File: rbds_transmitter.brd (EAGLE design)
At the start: 160 x 100 mm, 136 parts, among them J2 AVRISP-6, Q1 P-CH, Q2 P-Ch, Q3 P-Ch, T1 ATB3225-75032CT, T2 ATB3225-75032CT, U1 MAX2606, U2 TS974, U3 TS974, U4 MAX1551, U5 ATMEGA328, U6 TPS61030, U7 MCP4812, X1 16Mhz

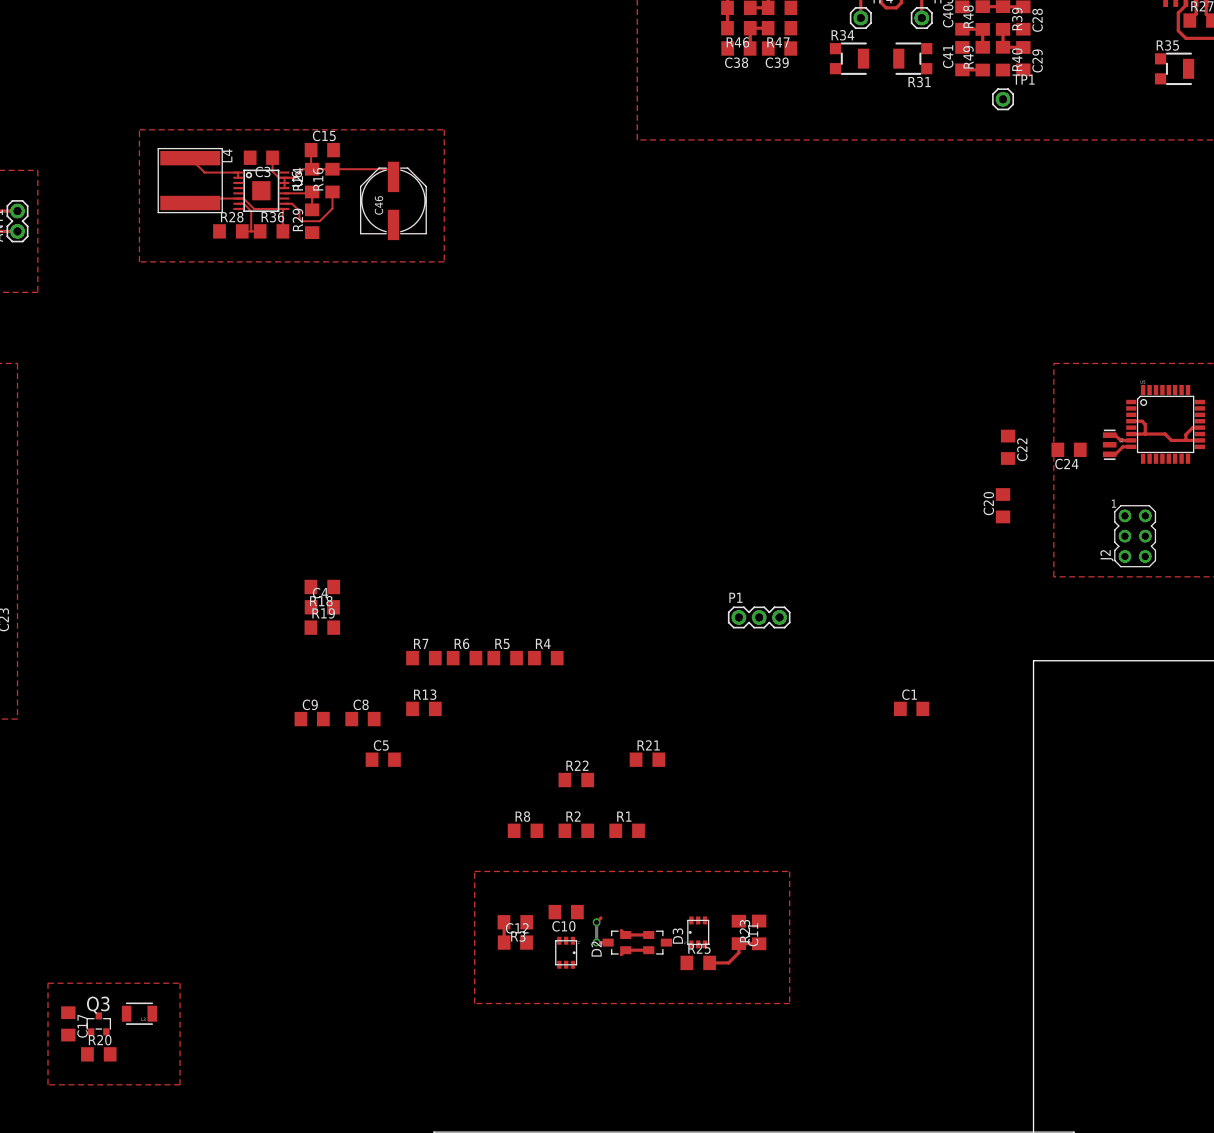
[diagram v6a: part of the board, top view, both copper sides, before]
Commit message: layed out some more traces
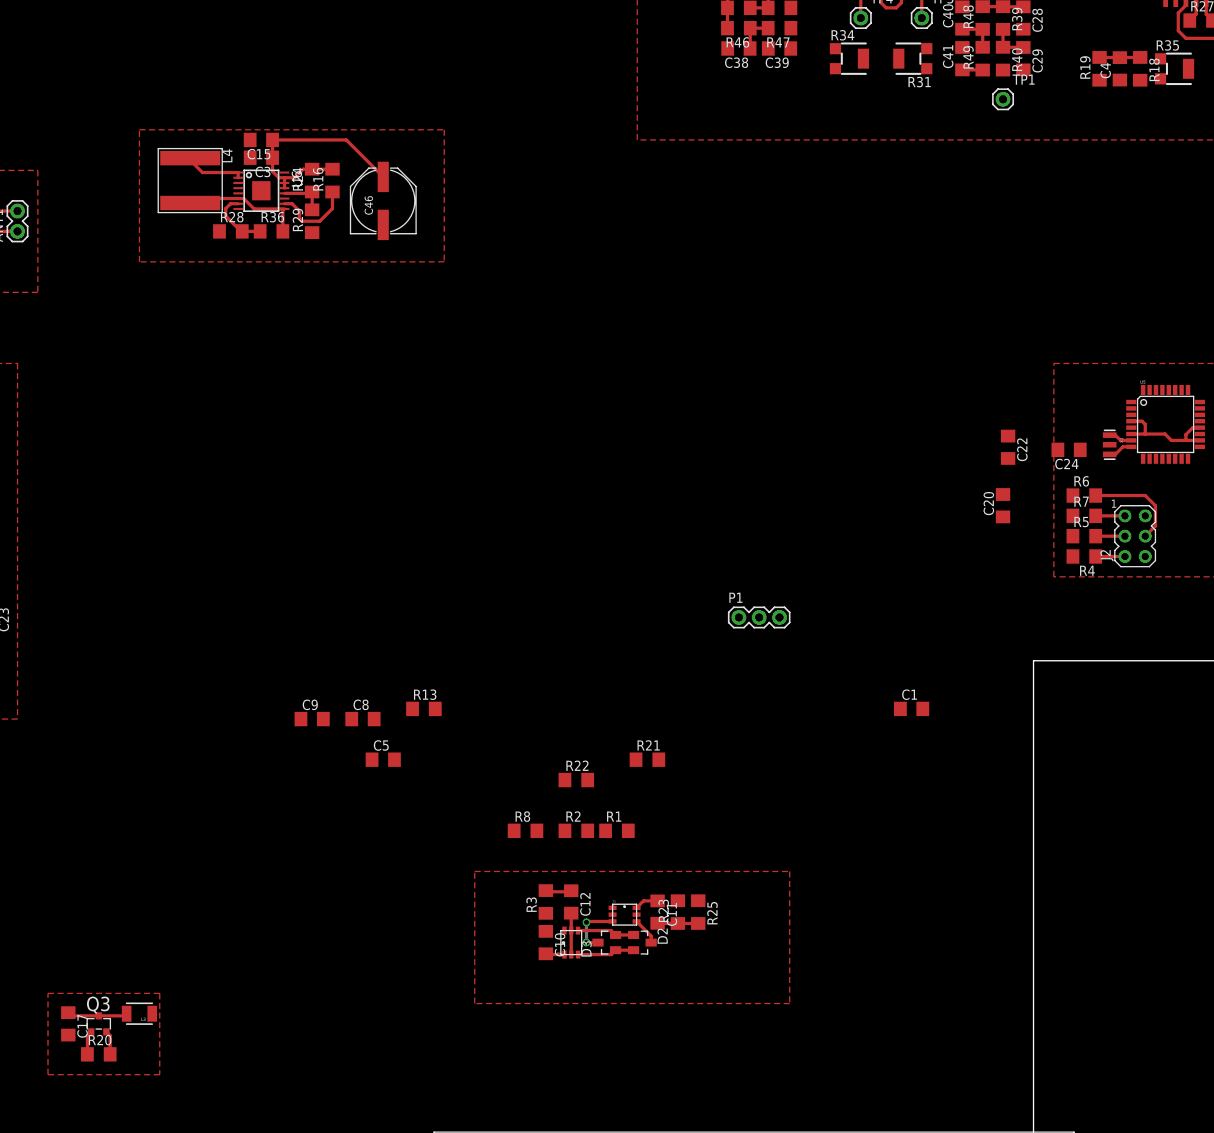
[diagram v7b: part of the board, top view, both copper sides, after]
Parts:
- C46: value 100uF -> (none)
- moved R18 121.0 mm to (13.3, 174.0), turned to 270 degrees
- moved C4 120.3 mm to (10.8, 174.0), turned to 90 degrees
- moved R19 119.7 mm to (8.26, 174.0), turned to 90 degrees
- moved R7 84.4 mm to (6.35, 118.1)
- moved R6 80.1 mm to (6.35, 120.7)
- moved R5 74.0 mm to (6.35, 115.6)
- moved R4 68.5 mm to (6.35, 113.0), turned to 180 degrees
- moved C11 10.5 mm to (-47.0, 68.6)
- moved R23 10.5 mm to (-44.5, 68.6)
- moved T2 9.47 mm to (-51.1, 68.3), turned to 0 degrees
- moved C12 8.64 mm to (-57.8, 69.8), turned to 270 degrees
- moved C15 7.73 mm to (-96.5, 165.1), turned to 180 degrees
- moved D3 6.35 mm to (-53.3, 64.8), turned to 90 degrees
- moved R25 6.35 mm to (-41.9, 68.6), turned to 270 degrees
- moved C10 4.58 mm to (-61.0, 64.8), turned to 270 degrees
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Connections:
- net +5V: now also C46.+
- net GND: now also C46.-
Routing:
- net ISP-MOSI: track 0.00 -> 12.3 mm
- net +5V: track 39.6 -> 50.1 mm
- net N$21: track 0.00 -> 7.57 mm
- net N$14: track 0.12 -> 7.28 mm, vias 0 -> 2
- net N$5: track 0.00 -> 5.28 mm
- net N$19: track 0.13 -> 5.18 mm
- net ISP-SCK: track 0.00 -> 3.66 mm
- net ISP-MISO: track 0.00 -> 3.66 mm
- net !ISP-RST: track 0.00 -> 3.66 mm
- net N$18: track 3.66 -> 7.17 mm
- net N$16: track 3.66 -> 7.17 mm
- net !TX_EN: track 0.00 -> 3.01 mm
- net RBDS: track 7.87 -> 5.09 mm
- net N$42: track 0.90 -> 2.99 mm
- net N$20: track 0.49 -> 2.42 mm
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
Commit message: swapped u3c and u3d
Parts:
- moved LCD1 240.3 mm to (-255.3, 163.8)
- moved C13 229.9 mm to (-244.8, 192.1)
- moved Q2 229.9 mm to (-248.6, 192.1)
- moved R17 229.9 mm to (-248.6, 188.3)
- moved R9 229.9 mm to (-242.3, 192.1)
- moved U5 156.8 mm to (-134.6, 171.4)
- moved X1 156.8 mm to (-141.6, 168.9)
- moved J2 154.3 mm to (-134.6, 161.3), turned to 90 degrees
- moved R6 150.0 mm to (-139.7, 154.9), turned to 90 degrees
- moved R7 148.2 mm to (-137.2, 154.9), turned to 90 degrees
- moved C22 147.4 mm to (-142.9, 173.7)
- moved R5 146.4 mm to (-134.6, 154.9), turned to 90 degrees
- moved R4 144.6 mm to (-132.1, 154.9), turned to 270 degrees
- moved TP3 140.2 mm to (-94.0, 114.3)
- moved C24 138.6 mm to (-127.6, 168.3), turned to 270 degrees
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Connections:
- net BPSK: now also U3.13, U3.14; no longer U3.8, U3.9
- net FREQUENCY: now also U3.8, U3.9; no longer U3.13, U3.14
- net N$28: now also U3.12; no longer U3.10
- net N$46: now also U3.10; no longer U3.12
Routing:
- net VCC: track 46.0 -> 137.0 mm, vias 0 -> 4
- net N$76: track 3.75 -> 77.0 mm, vias 0 -> 1
- net N$71: track 3.81 -> 69.9 mm, vias 0 -> 1
- net N$65: track 3.75 -> 38.9 mm, vias 0 -> 1
- net FREQUENCY: track 5.02 -> 29.4 mm, vias 0 -> 1
- net N$23: track 0.00 -> 23.3 mm
- net N$75: track 0.00 -> 18.9 mm
- net N$22: track 0.00 -> 18.4 mm
- net N$82: track 3.75 -> 18.5 mm
- net N$50: track 15.6 -> 29.8 mm
- net +5V: track 50.1 -> 61.1 mm
- net N$74: track 2.73 -> 12.4 mm
- net RBDS: track 5.09 -> 14.7 mm
- net N$64: track 0.00 -> 9.49 mm
- net N$77: track 0.00 -> 8.97 mm
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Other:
- board size 160 x 100 mm -> 80 x 100 mm
